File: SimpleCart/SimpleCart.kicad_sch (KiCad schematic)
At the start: 9 parts, among them J1 CommanderX16Expansion Alt, U1 SST39SF040, U2 74HCT00, U3 74HCT138

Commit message: BOM, fully routed
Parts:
- C1, C2, C3: value C -> 100nF; footprint Capacitor_THT:C_Disc_D5.0mm_W2.5mm_P5.00mm -> Capacitor_THT:C_Axial_L3.8mm_D2.6mm_P7.50mm_Horizontal
- JP1: value Jumper_2_Bridged -> WRITE EN
- R1: value R -> 4.7k
- U1: value SST39SF040 -> SST39SF040 (ROM)
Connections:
- net !ROMBEN: now also U3.15 (~{Y0}); no longer U3.14 (~{Y1})
- net ROMB4: now reaches J1.22 (ROMB4), U1.1 (A18)
- net A2: now reaches J1.35 (A2), U1.10 (A2)
- net A1: now reaches J1.33 (A1), U1.11 (A1)
- net A0: now reaches J1.31 (A0), U1.12 (A0)
- net D0: now reaches J1.30 (D0), U1.13 (D0)
- net D1: now reaches J1.32 (D1), U1.14 (D1)
- net D2: now reaches J1.34 (D2), U1.15 (D2)
- net D3: now reaches J1.36 (D3), U1.17 (D3)
- net D4: now reaches J1.38 (D4), U1.18 (D4)
- net D5: now reaches J1.40 (D5), U1.19 (D5)
- net ROMB2: now reaches J1.16 (ROMB2), U1.2 (A16)
- net D6: now reaches J1.42 (D6), U1.20 (D6)
- net D7: now reaches J1.44 (D7), U1.21 (D7)
- net A10: now reaches J1.51 (A10), U1.23 (A10)
- net A11: now reaches J1.53 (A11), U1.25 (A11)
- net A9: now reaches J1.49 (A9), U1.26 (A9)
- net A8: now reaches J1.47 (A8), U1.27 (A8)
- net A13: now reaches J1.50 (A13), U1.28 (A13)
- net ROMB0: now reaches J1.10 (ROMB0), U1.29 (A14)
- net ROMB1: now reaches J1.12 (ROMB1), U1.3 (A15)
- net ROMB3: now reaches J1.20 (ROMB3), U1.30 (A17)
- net A12: now reaches J1.52 (A12), U1.4 (A12)
- net A7: now reaches J1.45 (A7), U1.5 (A7)
- net A6: now reaches J1.43 (A6), U1.6 (A6)
- net A5: now reaches J1.41 (A5), U1.7 (A5)
- net A4: now reaches J1.39 (A4), U1.8 (A4)
- net A3: now reaches J1.37 (A3), U1.9 (A3)
- new net !RAMBEN: U3.14 (~{Y1})
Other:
- moved on the sheet: C1, JP1, R1, U1

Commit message: Polish and a readme explaining WTF
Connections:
- net !RAMBEN renamed !CHIP1EN
- net !CHIP1EN: now also U1.22 (CE)
- net !ROMBEN: no longer names the net of U3.15 (~{Y0})
- net !ROMBEN: no longer U1.22 (CE)
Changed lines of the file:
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@@
 	(wire
 		(pts
-			(xy 243.84 40.64) (xy 237.49 40.64)
+			(xy 214.63 53.34) (xy 217.17 53.34)
 		)
 		(stroke
@@
 	(wire
 		(pts
-			(xy 214.63 53.34) (xy 217.17 53.34)
+			(xy 213.36 85.09) (xy 215.9 85.09)
 		)
 		(stroke
@@
 	(wire
 		(pts
-			(xy 213.36 85.09) (xy 215.9 85.09)
+			(xy 213.36 90.17) (xy 213.36 85.09)
 		)
 		(stroke
@@
 	(wire
 		(pts
-			(xy 213.36 90.17) (xy 213.36 85.09)
+			(xy 132.08 101.6) (xy 132.08 104.14)
 		)
 		(stroke
@@
 		)
 	)
-	(wire
-		(pts
-			(xy 237.49 43.18) (xy 243.84 43.18)
-		)
-		(stroke
-			(width 0)
-			(type default)
-		)
-	)
-	(wire
-		(pts
-			(xy 132.08 101.6) (xy 132.08 104.14)
-		)
-		(stroke
-			(width 0)
-			(type default)
-		)
-	)
 	(global_label "ROMB4"
 		(shape input)
@@
 		)
 	)
-	(global_label "!ROMBEN"
+	(global_label "!CHIP1EN"
 		(shape input)
 		(at 58.42 180.34 180)
@@
 		)
 		(property "Intersheetrefs" "${INTERSHEET_REFS}"
-			(at 47.0286 180.34 0)
+			(at 46.6657 180.34 0)
 			(effects
 				(font
@@
 		)
 	)
-	(global_label "!ROMBEN"
-		(shape input)
-		(at 243.84 40.64 0)
-		(fields_autoplaced yes)
-		(effects
-			(font
-				(size 1.27 1.27)
-			)
-			(justify left)
-		)
-		(property "Intersheetrefs" "${INTERSHEET_REFS}"
-			(at 255.2314 40.64 0)
+	(global_label "!CHIP1EN"
+		(shape input)
+		(at 237.49 43.18 0)
+		(fields_autoplaced yes)
+		(effects
+			(font
+				(size 1.27 1.27)
+			)
+			(justify left)
+		)
+		(property "Intersheetrefs" "${INTERSHEET_REFS}"
+			(at 249.2443 43.18 0)
 			(effects
 				(font
@@
 				(hide yes)
 			)
-		)
-	)
-	(global_label "!RAMBEN"
-		(shape input)
-		(at 243.84 43.18 0)
-		(fields_autoplaced yes)
-		(effects
-			(font
-				(size 1.27 1.27)
-			)
-			(justify left)
-		)
-		(property "Intersheetrefs" "${INTERSHEET_REFS}"
-			(at 254.9895 43.18 0)
-			(effects
-				(font
-					(size 1.27 1.27)
-				)
-				(justify left)
-				(hide yes)
-			)

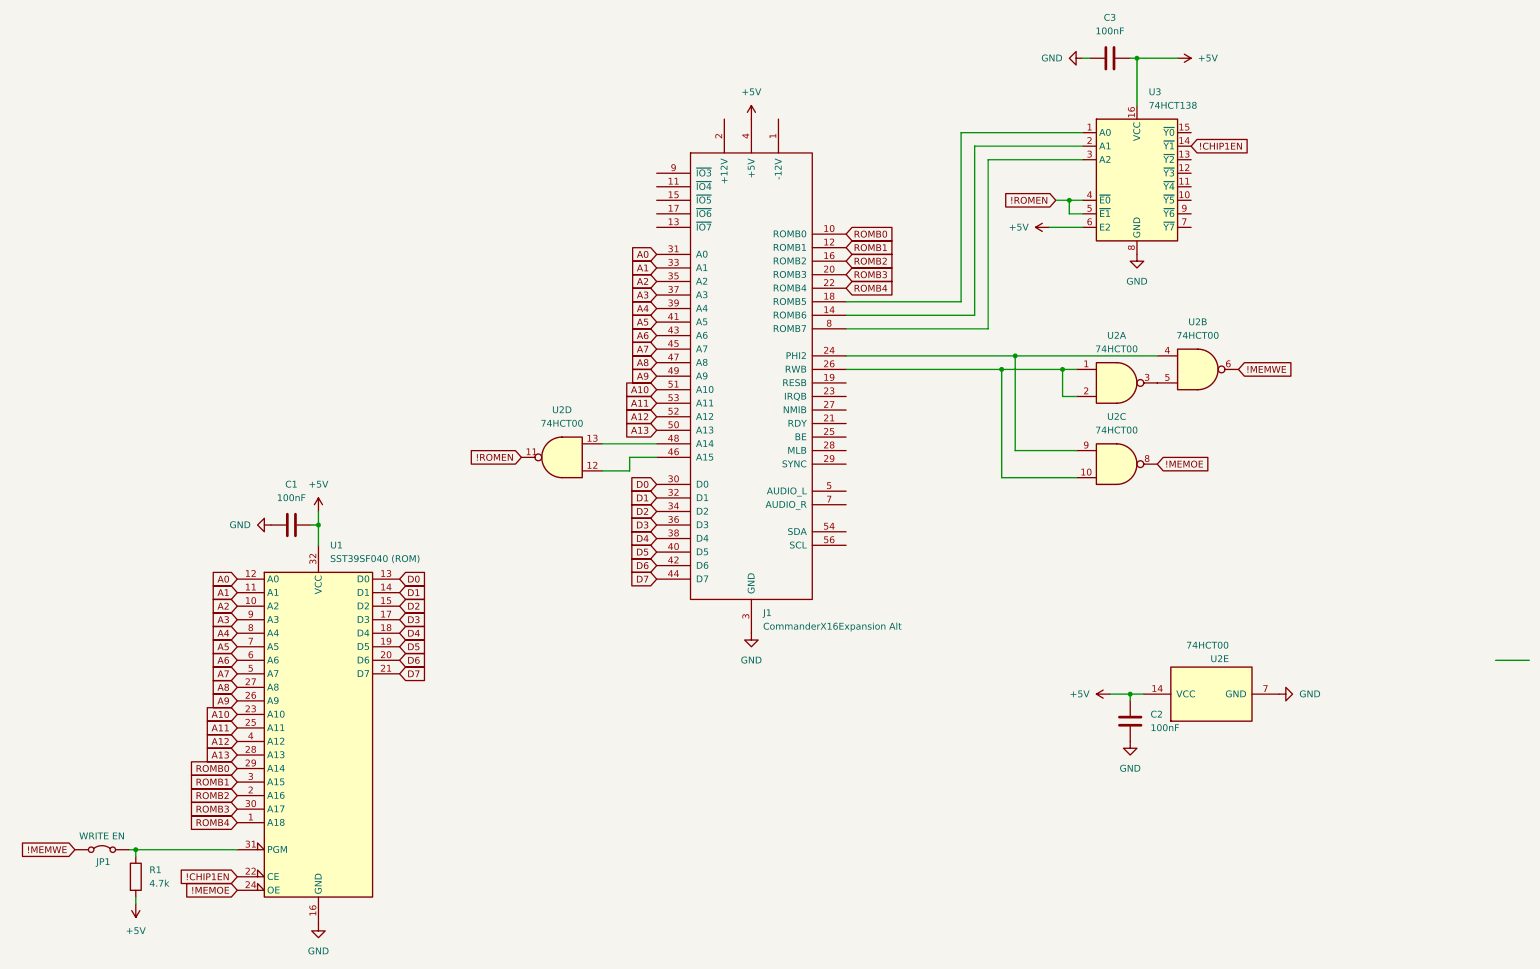
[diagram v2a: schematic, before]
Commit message: Tweaks to both Simplecart and ROAM
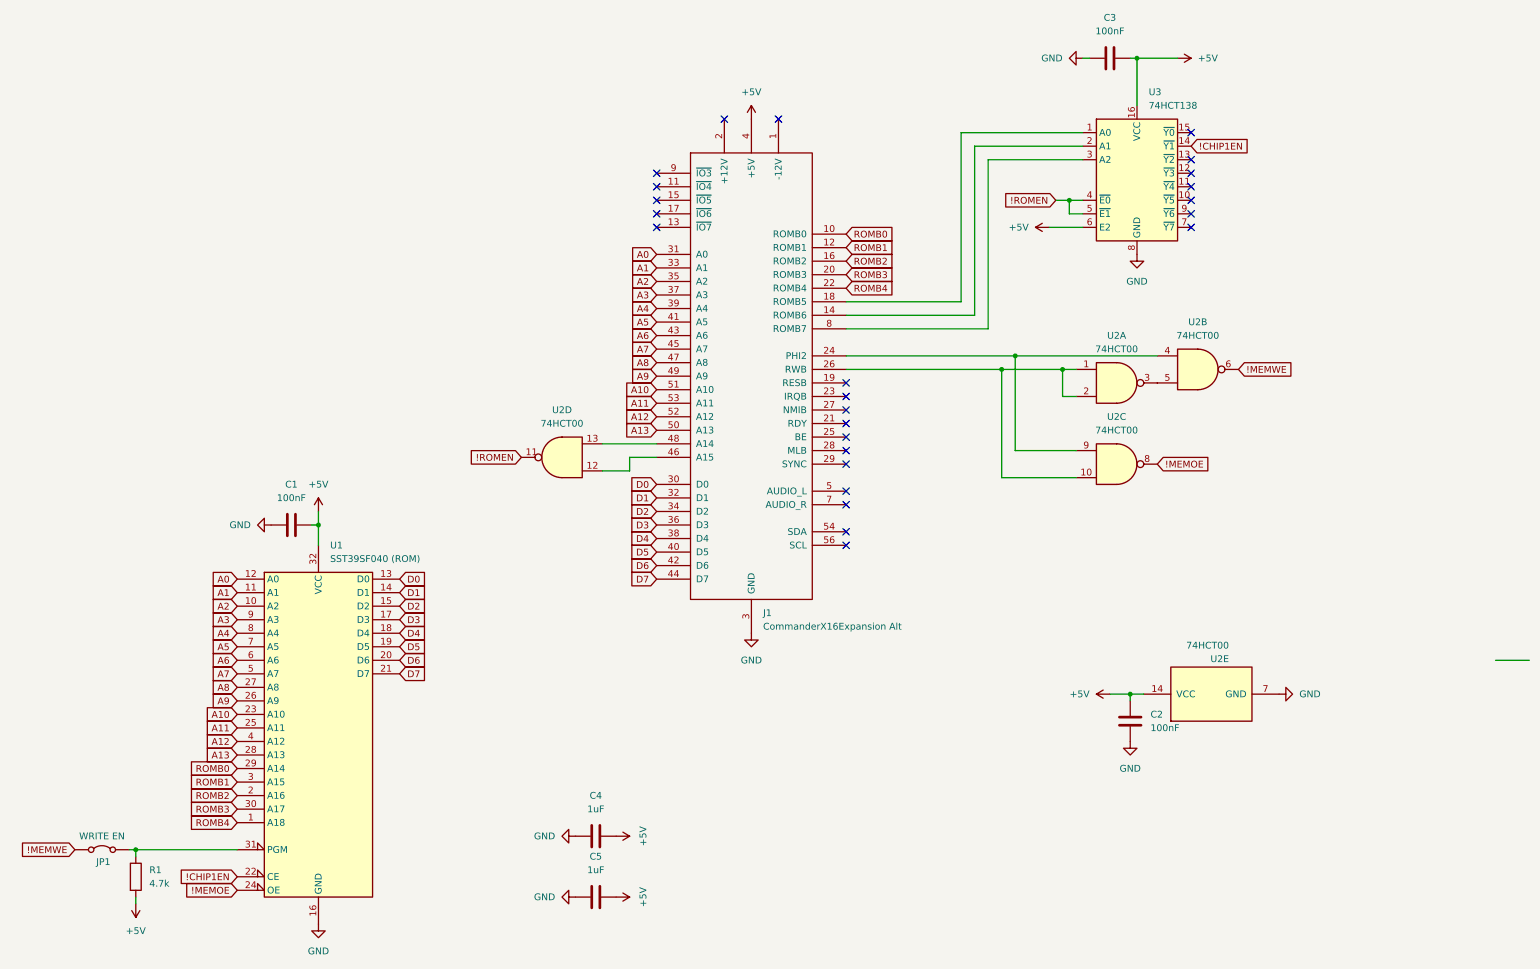
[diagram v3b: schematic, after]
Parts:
- added C4, C5: 1uF, Capacitor_THT:C_Disc_D4.3mm_W1.9mm_P5.00mm, symbol Device:C
- C1, C2, C3: footprint Capacitor_THT:C_Axial_L3.8mm_D2.6mm_P7.50mm_Horizontal -> Capacitor_THT:C_Disc_D4.3mm_W1.9mm_P5.00mm
- J1: footprint CommanderX16Expansion:CommanderX16Cartridge -> CommanderX16Expansion:CommanderX16SimpleCartridge
- R1: footprint Resistor_THT:R_Axial_DIN0204_L3.6mm_D1.6mm_P5.08mm_Horizontal -> Resistor_THT:R_Axial_DIN0204_L3.6mm_D1.6mm_P7.62mm_Horizontal
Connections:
- net +5V: now also C4.2, C5.2
- net GND: now also C4.1, C5.1
- no-connect marks 0 -> 25
